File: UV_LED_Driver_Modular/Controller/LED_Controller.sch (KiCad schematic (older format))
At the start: 9 parts, among them J1 Barrel_Jack, J2 Conn_01x05, SW1 SW_SPST, U1 STM32L011D4Px, U2 MCP1703A-3302_SOT223

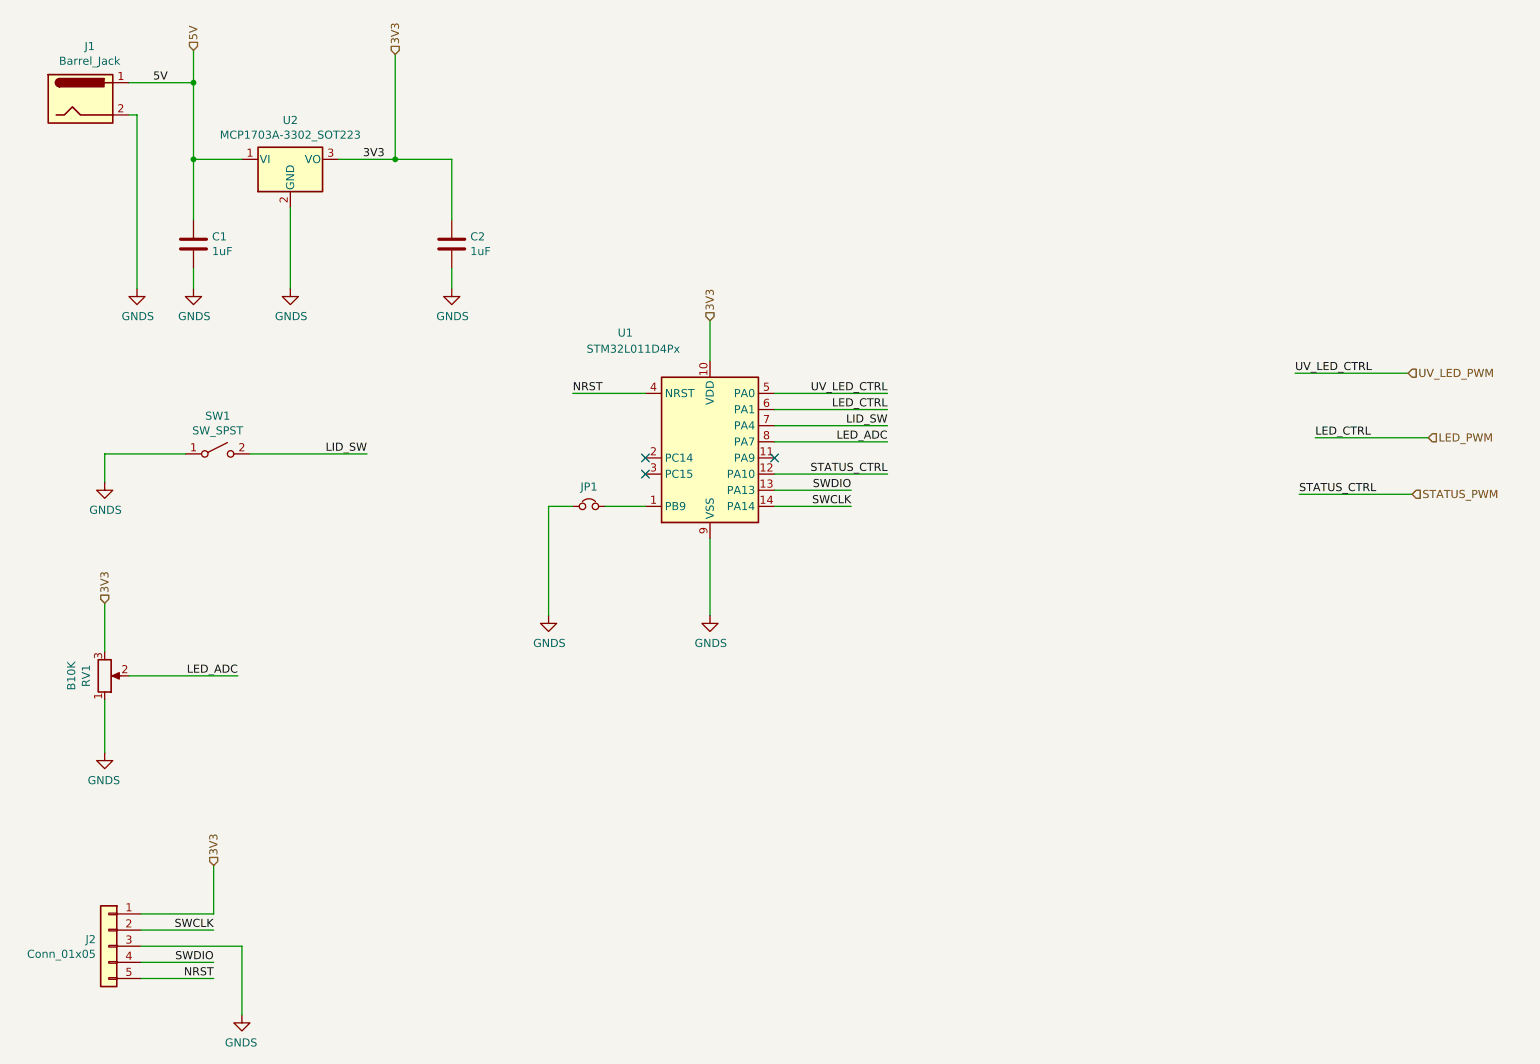
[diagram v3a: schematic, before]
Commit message: added IRS4427 mosfet gate driver to controller design
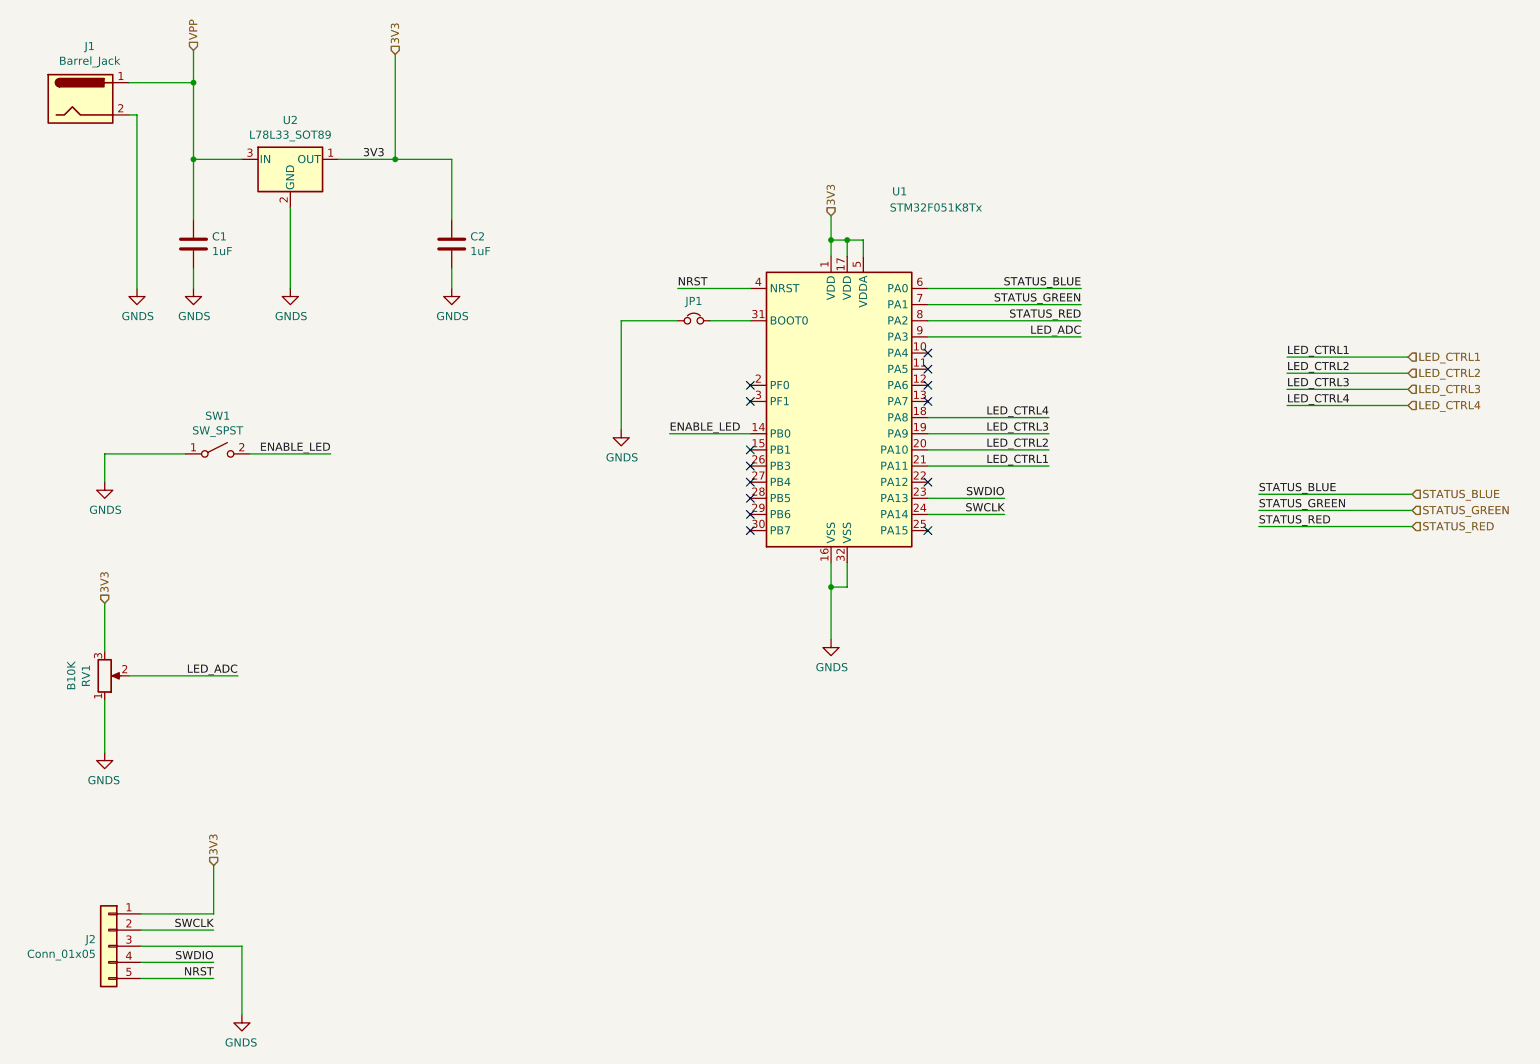
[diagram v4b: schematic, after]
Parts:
- removed U1: STM32L011D4Px, Package_SO:TSSOP-14_4.4x5mm_P0.65mm, symbol MCU_ST_STM32L0:STM32L011D4Px
- removed U2: MCP1703A-3302_SOT223, Package_TO_SOT_SMD:SOT-223-3_TabPin2, symbol Regulator_Linear:MCP1703A-3302_SOT223
- added U1: STM32F051K8Tx, Package_QFP:LQFP-32_7x7mm_P0.8mm, symbol MCU_ST_STM32F0:STM32F051K8Tx
- added U2: L78L33_SOT89, Package_TO_SOT_SMD:SOT-89-3, symbol Regulator_Linear:L78L33_SOT89
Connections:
- net 3V3: now also U1.1 (VDD), U1.17 (VDD), U1.5 (VDDA), U2.1 (OUT)
- net GNDS: now also U1.16 (VSS), U1.32 (VSS), U2.2 (GND)
- net LED_ADC: now also U1.9 (PA3)
- net NRST: now also U1.4 (NRST)
- net SWCLK: now also U1.24 (PA14)
- net SWDIO: now also U1.23 (PA13)
- net at JP1.2: now also U1.31 (BOOT0)
- net 5V renamed VPP
- net VPP: now also U2.3 (IN)
- net LID_SW renamed ENABLE_LED
- net ENABLE_LED: now also U1.14 (PB0)
- new net LED_CTRL1: U1.21 (PA11)
- new net LED_CTRL2: U1.20 (PA10)
- new net LED_CTRL3: U1.19 (PA9)
- new net LED_CTRL4: U1.18 (PA8)
- new net STATUS_BLUE: U1.6 (PA0)
- new net STATUS_GREEN: U1.7 (PA1)
- new net STATUS_RED: U1.8 (PA2)
- no-connect marks 3 -> 14
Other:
- moved on the sheet: JP1
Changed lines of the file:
@@
 	-1   0    0    -1
 $EndComp
-Text Label 4675 3275 0    50   ~ 0
+Text Label 5325 2625 0    50   ~ 0
 NRST
 Wire Wire Line
-	5125 3275 4675 3275
-Wire Wire Line
-	4525 3975 4525 4650
+	5775 2625 5325 2625
+Wire Wire Line
+	4975 2825 4975 3500
 $Comp
 L power:GNDS #PWR021
 U 1 1 5EA63B43
-P 4525 4650
-F 0 "#PWR021" H 4525 4400 50  0001 C CNN
-F 1 "GNDS" H 4530 4477 50  0000 C CNN
-F 2 "" H 4525 4650 50  0001 C CNN
-F 3 "" H 4525 4650 50  0001 C CNN
-	1    4525 4650
-	1    0    0    -1
-$EndComp
-NoConn ~ 5125 3775
-NoConn ~ 5125 3675
-NoConn ~ 5925 3675
-Wire Wire Line
-	5925 3875 6400 3875
-$Comp
-L MCU_ST_STM32L0:STM32L011D4Px U1
-U 1 1 5EA63B4E
-P 5525 3575
-F 0 "U1" H 5000 4250 50  0000 C CNN
-F 1 "STM32L011D4Px" H 5050 4150 50  0000 C CNN
-F 2 "Package_SO:TSSOP-14_4.4x5mm_P0.65mm" H 5225 3075 50  0001 R CNN
-F 3 "http://www.st.com/st-web-ui/static/active/en/resource/technical/document/datasheet/DM00206508.pdf" H 5525 3575 50  0001 C CNN
-	1    5525 3575
-	1    0    0    -1
-$EndComp
-Wire Wire Line
-	5925 3975 6400 3975
-Text Label 6400 3975 2    50   ~ 0
+P 4975 3500
+F 0 "#PWR021" H 4975 3250 50  0001 C CNN
+F 1 "GNDS" H 4980 3327 50  0000 C CNN
+F 2 "" H 4975 3500 50  0001 C CNN
+F 3 "" H 4975 3500 50  0001 C CNN
+	1    4975 3500
+	1    0    0    -1
+$EndComp
+Wire Wire Line
+	6875 3925 7350 3925
+Wire Wire Line
+	6875 4025 7350 4025
+Text Label 7350 4025 2    50   ~ 0
 SWCLK
-Text Label 6400 3875 2    50   ~ 0
+Text Label 7350 3925 2    50   ~ 0
 SWDIO
 Wire Wire Line
-	5525 3075 5525 2825
-Wire Wire Line
-	5525 4175 5525 4650
+	6275 2425 6275 2325
+Wire Wire Line
+	6275 4325 6275 4475
 $Comp
 L power:GNDS #PWR022
 U 1 1 5EA63B5F
-P 5525 4650
-F 0 "#PWR022" H 5525 4400 50  0001 C CNN
-F 1 "GNDS" H 5530 4477 50  0000 C CNN
-F 2 "" H 5525 4650 50  0001 C CNN
-F 3 "" H 5525 4650 50  0001 C CNN
-	1    5525 4650
+P 6275 4800
+F 0 "#PWR022" H 6275 4550 50  0001 C CNN
+F 1 "GNDS" H 6280 4627 50  0000 C CNN
+F 2 "" H 6275 4800 50  0001 C CNN
+F 3 "" H 6275 4800 50  0001 C CNN
+	1    6275 4800
 	1    0    0    -1
 $EndComp
@@
 $EndComp
 Wire Wire Line
-	2675 3650 3400 3650
-Text Label 3400 3650 2    50   ~ 0
-LID_SW
-Wire Wire Line
-	5925 3475 6625 3475
-Text Label 6625 3475 2    50   ~ 0
-LID_SW
-Wire Wire Line
 	2625 1825 2325 1825
 Connection ~ 2325 1825
@@
 	2325 1350 2325 1150
 Connection ~ 2325 1350
-Wire Wire Line
-	5925 3275 6625 3275
-Text Label 6625 3275 2    50   ~ 0
-UV_LED_CTRL
-Wire Wire Line
-	5925 3375 6625 3375
-Text Label 6625 3375 2    50   ~ 0
-LED_CTRL
-Wire Wire Line
-	5925 3575 6625 3575
-Text Label 6625 3575 2    50   ~ 0
-LED_ADC
 $Comp
 L Device:R_POT RV1
@@
 Wire Wire Line
 	1775 4875 1775 4575
-Text Label 2600 5025 2    50   ~ 0
-LED_ADC
 Text HLabel 9850 3150 2    50   Input ~ 0
-UV_LED_PWM
-Text HLabel 9975 3550 2    50   Input ~ 0
-LED_PWM
-Wire Wire Line
-	9850 3150 9150 3150
-Text Label 9150 3150 0    50   ~ 0
-UV_LED_CTRL
-Wire Wire Line
-	9975 3550 9275 3550
-Text Label 9275 3550 0    50   ~ 0
-LED_CTRL
+LED_CTRL2
 Text HLabel 2325 1150 1    50   Input ~ 0
-5V
+VPP
 Text HLabel 3575 1175 1    50   Input ~ 0
 3V3
 Text Label 3375 1825 0    50   ~ 0
 3V3
-Text HLabel 5525 2825 1    50   Input ~ 0
+Text HLabel 6275 2175 1    50   Input ~ 0
 3V3
 Text HLabel 1775 4575 1    50   Input ~ 0
@@
 Text HLabel 2450 6200 1    50   Input ~ 0
 3V3
-Text Label 2075 1350 0    50   ~ 0
-5V
 Wire Wire Line
 	1975 1550 1975 2625
@@
 $EndComp
 Wire Wire Line
-	4525 3975 4675 3975
-Wire Wire Line
-	4875 3975 5125 3975
+	4975 2825 5325 2825
+Wire Wire Line
+	5525 2825 5775 2825
 $Comp
 L Device:Jumper_NC_Small JP1
 U 1 1 5EA6AD24
-P 4775 3975
-F 0 "JP1" H 4775 4096 50  0000 C CNN
-F 1 "Jumper_NC_Small" H 4775 4096 50  0001 C CNN
-F 2 "Jumper:SolderJumper-2_P1.3mm_Bridged_Pad1.0x1.5mm" H 4775 3975 50  0001 C CNN
-F 3 "~" H 4775 3975 50  0001 C CNN
-	1    4775 3975
-	1    0    0    -1
-$EndComp
-Wire Wire Line
-	5925 3775 6625 3775
-Text Label 6625 3775 2    50   ~ 0
-STATUS_CTRL
-Wire Wire Line
-	9875 3900 9175 3900
-Text Label 9175 3900 0    50   ~ 0
-STATUS_CTRL
-Text HLabel 9875 3900 2    50   Input ~ 0
-STATUS_PWM
-$Comp
-L Regulator_Linear:MCP1703A-3302_SOT223 U2
-U 1 1 5EAEE911
+P 5425 2825
+F 0 "JP1" H 5425 2946 50  0000 C CNN
+F 1 "Jumper_NC_Small" H 5425 2946 50  0001 C CNN
+F 2 "Jumper:SolderJumper-2_P1.3mm_Bridged_Pad1.0x1.5mm" H 5425 2825 50  0001 C CNN
+F 3 "~" H 5425 2825 50  0001 C CNN
+	1    5425 2825
+	1    0    0    -1
+$EndComp
+Text HLabel 9875 4100 2    50   Input ~ 0
+STATUS_RED
+Wire Wire Line
+	2325 1825 2325 2200
+Connection ~ 3575 1825
+$Comp
+L Regulator_Linear:L78L33_SOT89 U2
+U 1 1 5EA8E5E2
 P 2925 1825
 F 0 "U2" H 2925 2067 50  0000 C CNN
-F 1 "MCP1703A-3302_SOT223" H 2925 1976 50  0000 C CNN
-F 2 "Package_TO_SOT_SMD:SOT-223-3_TabPin2" H 2925 2025 50  0001 C CNN
-F 3 "http://ww1.microchip.com/downloads/en/DeviceDoc/20005122B.pdf" H 2925 1775 50  0001 C CNN
+F 1 "L78L33_SOT89" H 2925 1976 50  0000 C CNN
+F 2 "Package_TO_SOT_SMD:SOT-89-3" H 2925 2025 50  0001 C CIN
+F 3 "http://www.st.com/content/ccc/resource/technical/document/datasheet/15/55/e5/aa/23/5b/43/fd/CD00000446.pdf/files/CD00000446.pdf/jcr:content/translations/en.CD00000446.pdf" H 2925 1775 50  0001 C CNN
 	1    2925 1825
 	1    0    0    -1
 $EndComp
-Wire Wire Line
-	2325 1825 2325 2200
-Connection ~ 3575 1825
+$Comp
+L MCU_ST_STM32F0:STM32F051K8Tx U1
+U 1 1 5EA919B4
+P 6375 3325
+F 0 "U1" H 6700 4625 50  0000 C CNN
+F 1 "STM32F051K8Tx" H 6925 4525 50  0000 C CNN
+F 2 "Package_QFP:LQFP-32_7x7mm_P0.8mm" H 5875 2425 50  0001 R CNN
+F 3 "http://www.st.com/st-web-ui/static/active/en/resource/technical/document/datasheet/DM00039193.pdf" H 6375 3325 50  0001 C CNN
+	1    6375 3325
+	1    0    0    -1
+$EndComp
+Wire Wire Line
+	6375 4325 6375 4475
+Wire Wire Line
+	6375 4475 6275 4475
+Connection ~ 6275 4475
+Wire Wire Line
+	6275 4475 6275 4800
+Wire Wire Line
+	6275 2325 6375 2325
+Wire Wire Line
+	6375 2325 6375 2425
+Connection ~ 6275 2325
+Wire Wire Line
+	6275 2325 6275 2175
+Wire Wire Line
+	6375 2325 6475 2325
+Wire Wire Line
+	6475 2325 6475 2425
+Connection ~ 6375 2325
+Wire Wire Line
+	6875 2625 7825 2625
+Text Label 7825 2625 2    50   ~ 0
+STATUS_BLUE
+Text Label 7825 2725 2    50   ~ 0
+STATUS_GREEN
+Wire Wire Line
+	6875 2725 7825 2725
+Text Label 7825 2825 2    50   ~ 0
+STATUS_RED
+Wire Wire Line
+	7825 2825 6875 2825
+Text Label 5275 3525 0    50   ~ 0
+ENABLE_LED
+Wire Wire Line
+	5275 3525 5775 3525
+Text Label 7625 3725 2    50   ~ 0
+LED_CTRL1
+Wire Wire Line
+	7625 3725 6875 3725
+Text Label 7625 3625 2    50   ~ 0
+LED_CTRL2
+Wire Wire Line
+	7625 3625 6875 3625
+Text Label 7625 3525 2    50   ~ 0
+LED_CTRL3
+Wire Wire Line
+	7625 3525 6875 3525
+Text Label 7625 3425 2    50   ~ 0
+LED_CTRL4
+Wire Wire Line
+	7625 3425 6875 3425
+NoConn ~ 6875 3025
+NoConn ~ 6875 3125
+NoConn ~ 6875 3225
+NoConn ~ 6875 3325
+NoConn ~ 6875 3825
+NoConn ~ 6875 4125
+NoConn ~ 5775 4125
+NoConn ~ 5775 4025
+NoConn ~ 5775 3925
+NoConn ~ 5775 3825
+NoConn ~ 5775 3725
+NoConn ~ 5775 3625
+NoConn ~ 5775 3325
+NoConn ~ 5775 3225
+Text Label 2600 5025 2    50   ~ 0
+LED_ADC
+Wire Wire Line
+	6875 2925 7825 2925
+Text Label 7825 2925 2    50   ~ 0
+LED_ADC
+Text HLabel 9850 3250 2    50   Input ~ 0
+LED_CTRL3
+Text HLabel 9850 3350 2    50   Input ~ 0
+LED_CTRL4
+Text HLabel 9850 3050 2    50   Input ~ 0
+LED_CTRL1
+Text HLabel 9875 4000 2    50   Input ~ 0
+STATUS_GREEN
+Text HLabel 9875 3900 2    50   Input ~ 0
+STATUS_BLUE
+Wire Wire Line
+	9875 3900 8925 3900
+Text Label 8925 3900 0    50   ~ 0
+STATUS_BLUE
+Text Label 8925 4000 0    50   ~ 0
+STATUS_GREEN
+Wire Wire Line
+	9875 4000 8925 4000
+Text Label 8925 4100 0    50   ~ 0
+STATUS_RED
+Wire Wire Line
+	8925 4100 9875 4100
+Text Label 9100 3050 0    50   ~ 0
+LED_CTRL1
+Wire Wire Line
+	9100 3050 9850 3050
+Text Label 9100 3150 0    50   ~ 0
+LED_CTRL2
+Wire Wire Line
+	9100 3150 9850 3150
+Text Label 9100 3250 0    50   ~ 0
+LED_CTRL3
+Wire Wire Line
+	9100 3250 9850 3250
+Text Label 9100 3350 0    50   ~ 0
+LED_CTRL4
+Wire Wire Line
+	9100 3350 9850 3350
+Text Label 3175 3650 2    50   ~ 0
+ENABLE_LED
+Wire Wire Line
+	3175 3650 2675 3650
 $EndSCHEMATC

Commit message: docs update
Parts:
- removed RV1: B10K, Connector_Molex:Molex_KK-254_AE-6410-03A_1x03_P2.54mm_Vertical, symbol Device:R_POT
- J2: footprint Connector_Molex:Molex_KK-254_AE-6410-05A_1x05_P2.54mm_Vertical -> Connector_PinHeader_2.54mm:PinHeader_1x05_P2.54mm_Vertical
- SW1: footprint Connector_Molex:Molex_KK-254_AE-6410-02A_1x02_P2.54mm_Vertical -> Connector_PinHeader_2.54mm:PinHeader_1x02_P2.54mm_Vertical
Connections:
- net LED_CTRL5: now reaches U1.15 (PB1)
- net ENC_B: now reaches U1.25 (PA15)
- net ENC_A: now reaches U1.26 (PB3)
- net LED_ADC: no longer names the net of U1.9 (PA3)
- no-connect marks 14 -> 12
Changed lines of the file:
@@
 $Descr A4 11693 8268
 encoding utf-8
-Sheet 2 2
+Sheet 2 3
 Title ""
 Date ""
@@
 F 0 "J2" H 1880 6742 50  0000 L CNN
 F 1 "Conn_01x05" H 1880 6651 50  0000 L CNN
-F 2 "Connector_Molex:Molex_KK-254_AE-6410-05A_1x05_P2.54mm_Vertical" H 1800 6700 50  0001 C CNN
+F 2 "Connector_PinHeader_2.54mm:PinHeader_1x05_P2.54mm_Vertical" H 1800 6700 50  0001 C CNN
 F 3 "~" H 1800 6700 50  0001 C CNN
 	1    1800 6700
@@
 	5775 2625 5325 2625
 Wire Wire Line
-	4975 2825 4975 3500
+	4625 2825 4625 3500
 $Comp
 L power:GNDS #PWR021
 U 1 1 5EA63B43
-P 4975 3500
-F 0 "#PWR021" H 4975 3250 50  0001 C CNN
-F 1 "GNDS" H 4980 3327 50  0000 C CNN
-F 2 "" H 4975 3500 50  0001 C CNN
-F 3 "" H 4975 3500 50  0001 C CNN
-	1    4975 3500
+P 4625 3500
+F 0 "#PWR021" H 4625 3250 50  0001 C CNN
+F 1 "GNDS" H 4630 3327 50  0000 C CNN
+F 2 "" H 4625 3500 50  0001 C CNN
+F 3 "" H 4625 3500 50  0001 C CNN
+	1    4625 3500
 	1    0    0    -1
 $EndComp
@@
 F 0 "SW1" H 2475 3885 50  0000 C CNN
 F 1 "SW_SPST" H 2475 3794 50  0000 C CNN
-F 2 "Connector_Molex:Molex_KK-254_AE-6410-02A_1x02_P2.54mm_Vertical" H 2475 3650 50  0001 C CNN
+F 2 "Connector_PinHeader_2.54mm:PinHeader_1x02_P2.54mm_Vertical" H 2475 3650 50  0001 C CNN
 F 3 "~" H 2475 3650 50  0001 C CNN
 	1    2475 3650
@@
 	2325 1350 2325 1150
 Connection ~ 2325 1350
-$Comp
-L Device:R_POT RV1
-U 1 1 5EA63BE5
-P 1775 5025
-F 0 "RV1" V 1660 5025 50  0000 C CNN
-F 1 "B10K" V 1569 5025 50  0000 C CNN
-F 2 "Connector_Molex:Molex_KK-254_AE-6410-03A_1x03_P2.54mm_Vertical" H 1775 5025 50  0001 C CNN
-F 3 "~" H 1775 5025 50  0001 C CNN
-	1    1775 5025
-	1    0    0    1
-$EndComp
-Wire Wire Line
-	1775 4875 1775 4575
 Text HLabel 9850 3150 2    50   Input ~ 0
 LED_CTRL2
@@
 Text HLabel 6275 2175 1    50   Input ~ 0
 3V3
-Text HLabel 1775 4575 1    50   Input ~ 0
-3V3
 Wire Wire Line
 	2450 6500 2450 6200
@@
 	1975 1550 1975 2625
 Wire Wire Line
-	1925 5025 2600 5025
-Wire Wire Line
-	1775 5175 1775 5500
-$Comp
-L power:GNDS #PWR0108
-U 1 1 5EB135AB
-P 1775 5500
-F 0 "#PWR0108" H 1775 5250 50  0001 C CNN
-F 1 "GNDS" H 1780 5327 50  0000 C CNN
-F 2 "" H 1775 5500 50  0001 C CNN
-F 3 "" H 1775 5500 50  0001 C CNN
-	1    1775 5500
-	-1   0    0    -1
-$EndComp
-Wire Wire Line
-	4975 2825 5325 2825
+	4625 2825 5325 2825
 Wire Wire Line
 	5525 2825 5775 2825
@@
 NoConn ~ 6875 3125
 NoConn ~ 6875 3225
-NoConn ~ 6875 3325
 NoConn ~ 6875 3825
-NoConn ~ 6875 4125
 NoConn ~ 5775 4125
 NoConn ~ 5775 4025
 NoConn ~ 5775 3925
 NoConn ~ 5775 3825
-NoConn ~ 5775 3725
-NoConn ~ 5775 3625
 NoConn ~ 5775 3325
 NoConn ~ 5775 3225
-Text Label 2600 5025 2    50   ~ 0
-LED_ADC
-Wire Wire Line
-	6875 2925 7825 2925
-Text Label 7825 2925 2    50   ~ 0
-LED_ADC
 Text HLabel 9850 3250 2    50   Input ~ 0
 LED_CTRL3
@@
 Wire Wire Line
 	3175 3650 2675 3650
+Wire Wire Line
+	5775 3625 5275 3625
+Text Label 5275 3625 0    50   ~ 0
+LED_CTRL5
+Wire Wire Line
+	9850 3450 9100 3450
+Text Label 9100 3450 0    50   ~ 0
+LED_CTRL5
+Text HLabel 9850 3450 2    50   Input ~ 0
+LED_CTRL5
+NoConn ~ 6875 3325
+$Sheet
+S 1600 4650 1075 750
+U 5EB5FCB1
+F0 "RotaryEncoderNoSwitch" 50
+F1 "RotaryEncoderNoSwitch.sch" 50
+F2 "ENC_PIN_A" I R 2675 5025 50
+F3 "ENC_PIN_B" I R 2675 5225 50
+F4 "3V3_ENC" I R 2675 4825 50
+$EndSheet
+Wire Wire Line
+	2675 5225 3175 5225
+Wire Wire Line
+	2675 5025 3175 5025
+Wire Wire Line
+	2675 4825 3175 4825
+Wire Wire Line
+	3175 4825 3175 4500
+Text HLabel 3175 4500 1    50   Input ~ 0
+3V3
+Text Label 3175 5025 2    50   ~ 0
+ENC_A
+Text Label 3175 5225 2    50   ~ 0
+ENC_B
+Wire Wire Line
+	6875 4125 7375 4125
+Wire Wire Line
+	5775 3725 5275 3725
+Text Label 5275 3725 0    50   ~ 0
+ENC_A
+Text Label 7375 4125 2    50   ~ 0
+ENC_B
+NoConn ~ 6875 2925
 $EndSCHEMATC
